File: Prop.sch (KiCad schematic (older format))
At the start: 12 parts

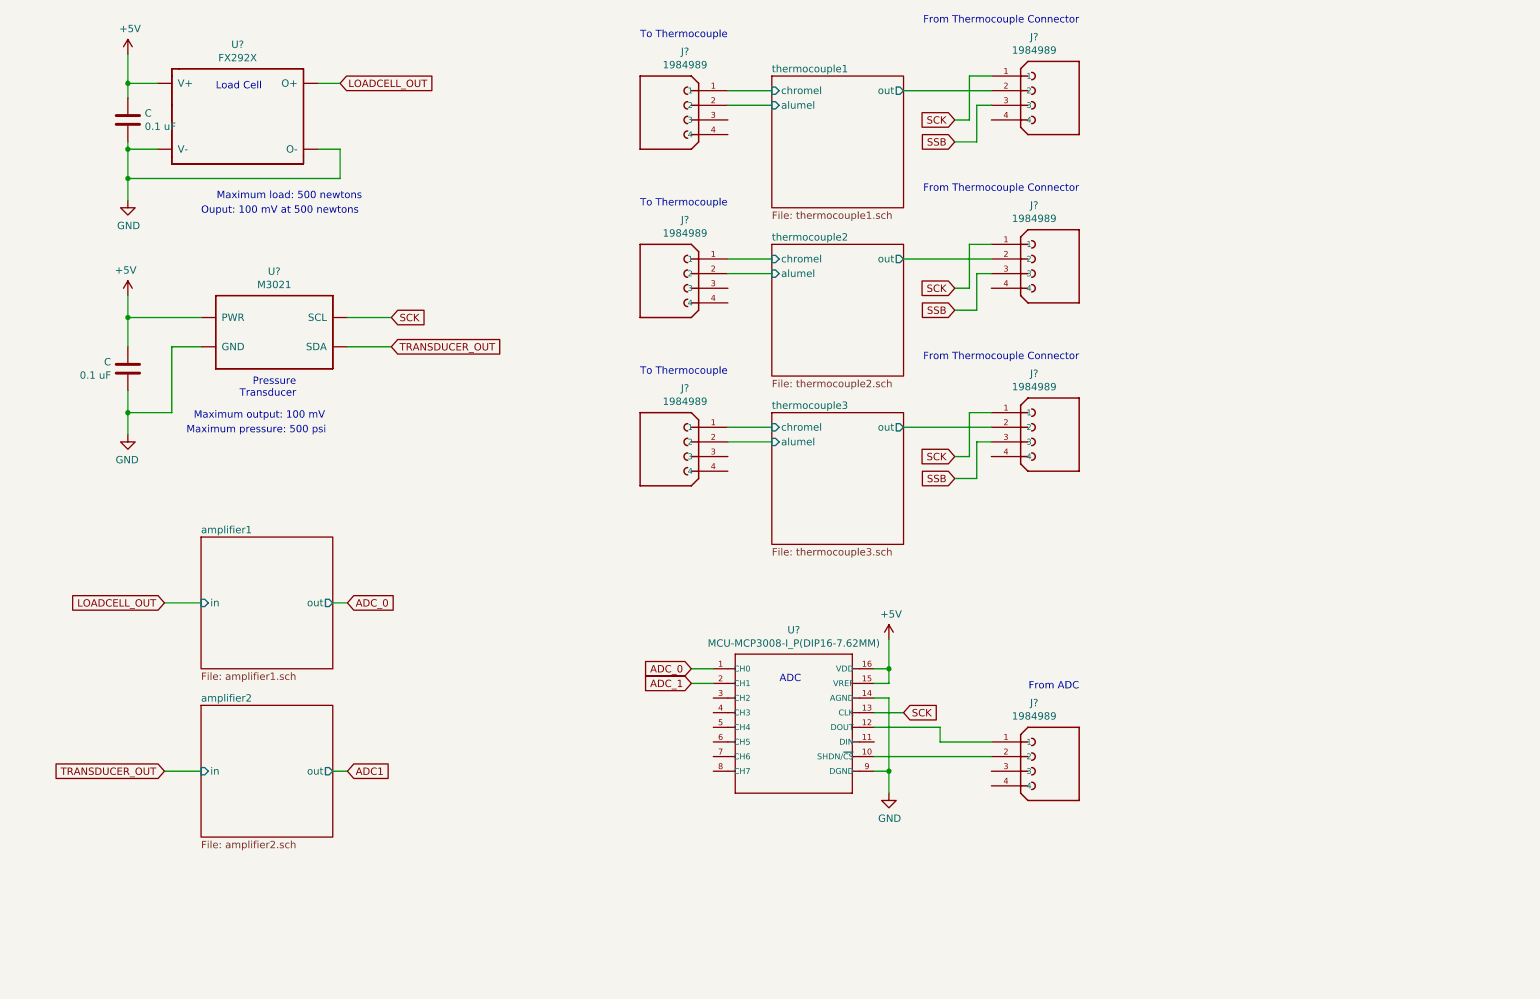
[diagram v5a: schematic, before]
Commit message: updated SCK
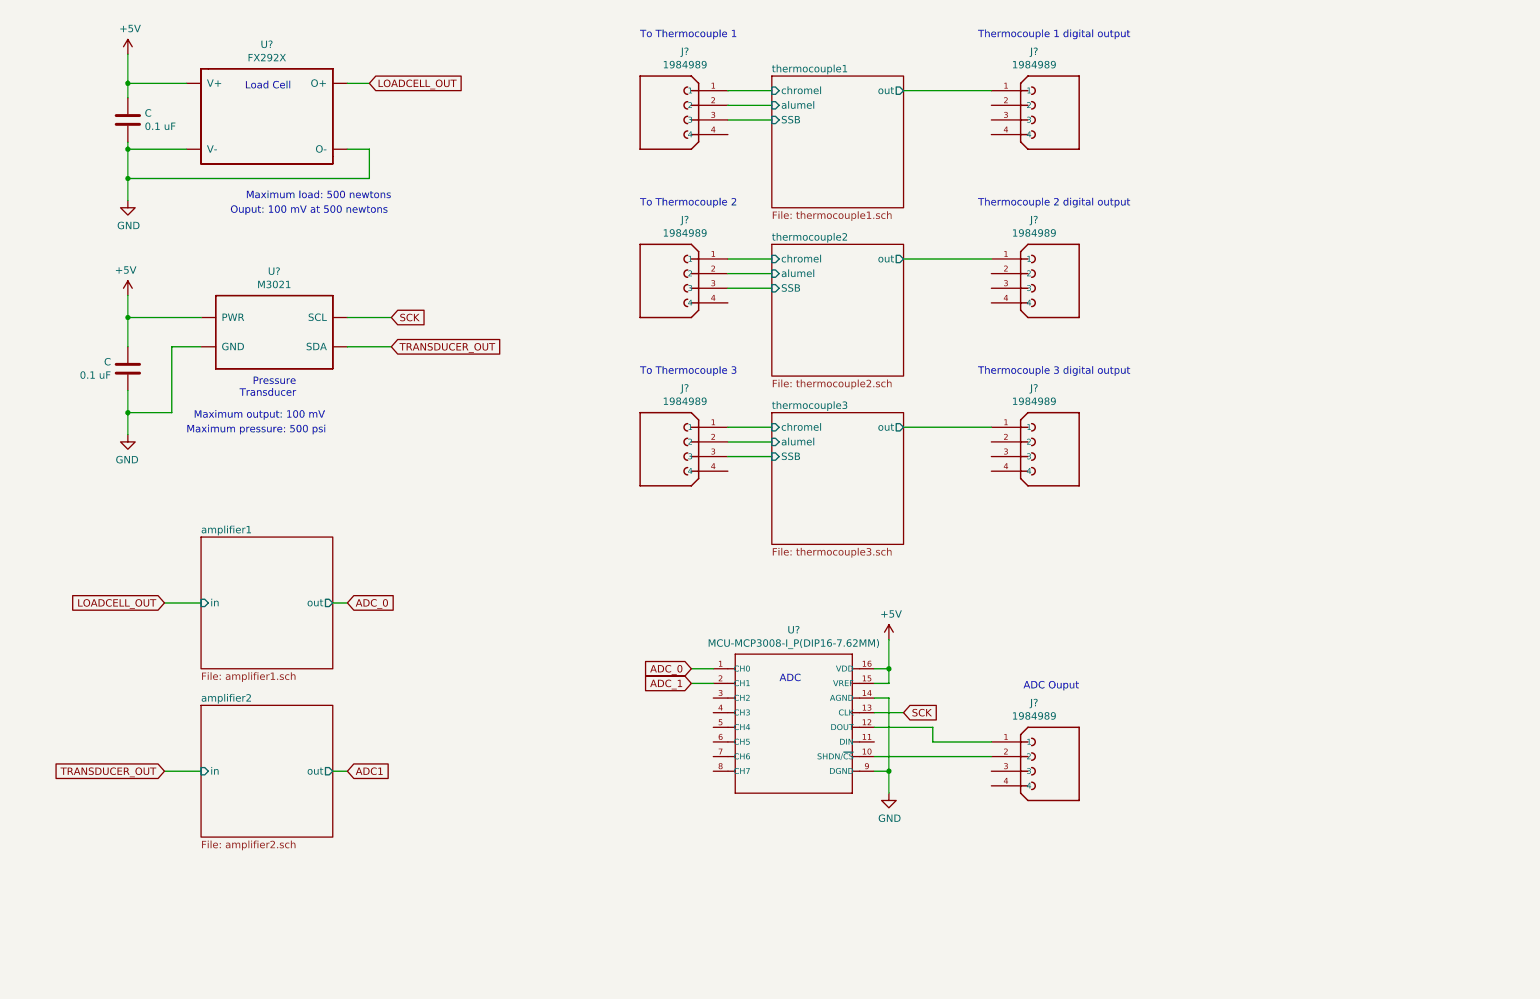
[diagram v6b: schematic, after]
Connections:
- net SCK: no longer J?.1, J?.1, J?.1
- net thermocouple1/out: now also J?.1; no longer J?.2
- net thermocouple2/out: now also J?.1; no longer J?.2
- net thermocouple3/out: now also J?.1; no longer J?.2
- net thermocouple1/SSB: now reaches J?.3
- net thermocouple2/SSB: now reaches J?.3
- net thermocouple3/SSB: now reaches J?.3
- removed net SSB: J?.3, J?.3, J?.3
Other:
- note added: "ADC Ouput"
- note added: "Thermocouple 1 digital output"
- note added: "Thermocouple 2 digital output"
- note added: "Thermocouple 3 digital output"
- note added: "To Thermocouple 1"
- note added: "To Thermocouple 2"
- note added: "To Thermocouple 3"
- note removed: "From ADC"
- note removed: "From Thermocouple Connector"
- note removed: "To Thermocouple"
- moved on the sheet: J?, U?
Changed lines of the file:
@@
 Connection ~ 1500 3400
 Wire Wire Line
-	2800 1150 2950 1150
+	3000 1150 3150 1150
 $Comp
 L power:+5V #PWR?
@@
 	1    0    0    -1
 $EndComp
-Text Notes 2100 1200 0    50   ~ 0
+Text Notes 2300 1200 0    50   ~ 0
 Load Cell
-Text GLabel 2950 1150 2    50   Input ~ 0
+Text GLabel 3150 1150 2    50   Input ~ 0
 LOADCELL_OUT
 $Comp
 L FX292X_Lib:FX292X U?
 U 1 1 603BDAFB
-P 2250 1250
-F 0 "U?" H 2250 1615 50  0000 C CNN
-F 1 "FX292X" H 2250 1524 50  0000 C CNN
-F 2 "" H 2250 1250 50  0001 C CNN
-F 3 "" H 2250 1250 50  0001 C CNN
-	1    2250 1250
+P 2450 1250
+F 0 "U?" H 2450 1615 50  0000 C CNN
+F 1 "FX292X" H 2450 1524 50  0000 C CNN
+F 2 "" H 2450 1250 50  0001 C CNN
+F 3 "" H 2450 1250 50  0001 C CNN
+	1    2450 1250
 	1    0    0    -1
 $EndComp
@@
 L 1984989:1984989 J?
 U 1 1 6041FC25
-P 7800 1200
-F 0 "J?" H 7907 1567 50  0000 C CNN
-F 1 "1984989" H 7907 1476 50  0000 C CNN
-F 2 "PHOENIX_1984989" H 7800 1200 50  0001 L BNN
-F 3 "" H 7800 1200 50  0001 L BNN
-F 4 "Phoenix Contact" H 7800 1200 50  0001 L BNN "MANUFACTURER"
-F 5 "2018-11-03" H 7800 1200 50  0001 L BNN "PARTREV"
-F 6 "13.1mm" H 7800 1200 50  0001 L BNN "MAXIMUM_PACKAGE_HEIGHT"
-F 7 "Manufacturer recommendations" H 7800 1200 50  0001 L BNN "STANDARD"
-	1    7800 1200
-	-1   0    0    -1
-$EndComp
-Text GLabel 7150 1400 0    50   Input ~ 0
-SCK
-Text GLabel 7150 1550 0    50   Input ~ 0
-SSB
+P 7800 1300
+F 0 "J?" H 7907 1667 50  0000 C CNN
+F 1 "1984989" H 7907 1576 50  0000 C CNN
+F 2 "PHOENIX_1984989" H 7800 1300 50  0001 L BNN
+F 3 "" H 7800 1300 50  0001 L BNN
+F 4 "Phoenix Contact" H 7800 1300 50  0001 L BNN "MANUFACTURER"
+F 5 "2018-11-03" H 7800 1300 50  0001 L BNN "PARTREV"
+F 6 "13.1mm" H 7800 1300 50  0001 L BNN "MAXIMUM_PACKAGE_HEIGHT"
+F 7 "Manufacturer recommendations" H 7800 1300 50  0001 L BNN "STANDARD"
+	1    7800 1300
+	-1   0    0    -1
+$EndComp
 $Comp
 L 1984989:1984989 J?
@@
 $EndComp
 Text Notes 5000 850  0    50   ~ 0
-To Thermocouple
-Text Notes 8000 750  2    50   ~ 0
-From Thermocouple Connector
+To Thermocouple 1
+Text Notes 8350 850  2    50   ~ 0
+Thermocouple 1 digital output
 Text Notes 8000 5300 2    50   ~ 0
-From ADC
+ADC Ouput
 $Comp
 L Device:C C
@@
 $EndComp
 Wire Wire Line
-	1500 950  1500 1150
-Wire Wire Line
-	1700 1150 1500 1150
-Wire Wire Line
-	1500 1600 1700 1600
-Wire Wire Line
-	1500 1600 1500 1550
-Wire Wire Line
-	1500 1250 1500 1150
-Connection ~ 1500 1150
-Wire Wire Line
-	1500 1600 1500 1800
-Connection ~ 1500 1600
-Wire Wire Line
-	2800 1600 2950 1600
-Wire Wire Line
-	2950 1600 2950 1800
-Wire Wire Line
-	2950 1800 1500 1800
-Connection ~ 1500 1800
-Wire Wire Line
-	1500 1800 1500 1950
+	3000 1600 3150 1600
+Wire Wire Line
+	3150 1600 3150 1800
 $Comp
 L MCU-MCP3008-I_P_DIP16-7.62MM_:MCU-MCP3008-I_P(DIP16-7.62MM) U?
@@
 Text Notes 6100 5250 2    50   ~ 0
 ADC
-Text Notes 3100 1950 2    50   ~ 0
+Text Notes 3300 1950 2    50   ~ 0
 Maximum load: 500 newtons
-Text Notes 2000 2050 0    50   ~ 0
+Text Notes 2200 2050 0    50   ~ 0
 Ouput: 100 mV at 500 newtons
 Text GLabel 5350 5150 0    50   Input ~ 0
@@
 F3 "chromel" I L 5900 1200 50
 F4 "out" O R 6800 1200 50
+F5 "SSB" I L 5900 1400 50
 $EndSheet
 $Sheet
@@
 F3 "alumel" I L 5900 2450 50
 F4 "out" O R 6800 2350 50
+F5 "SSB" I L 5900 2550 50
 $EndSheet
 $Sheet
@@
 F3 "alumel" I L 5900 3600 50
 F4 "out" O R 6800 3500 50
+F5 "SSB" I L 5900 3700 50
 $EndSheet
 $Comp
@@
 	5900 2450 5600 2450
 Text Notes 5000 2000 0    50   ~ 0
-To Thermocouple
+To Thermocouple 2
 $Comp
 L 1984989:1984989 J?
@@
 	5900 3600 5600 3600
 Text Notes 5000 3150 0    50   ~ 0
-To Thermocouple
-Wire Wire Line
-	7150 1400 7250 1400
-Wire Wire Line
-	7250 1400 7250 1100
-Wire Wire Line
-	7250 1100 7400 1100
-Wire Wire Line
-	7400 1300 7300 1300
-Wire Wire Line
-	7300 1300 7300 1550
-Wire Wire Line
-	7300 1550 7150 1550
-Wire Wire Line
-	7400 1200 6800 1200
+To Thermocouple 3
 $Comp
 L 1984989:1984989 J?
 U 1 1 6054FBA1
-P 7800 2350
-F 0 "J?" H 7907 2717 50  0000 C CNN
-F 1 "1984989" H 7907 2626 50  0000 C CNN
-F 2 "PHOENIX_1984989" H 7800 2350 50  0001 L BNN
-F 3 "" H 7800 2350 50  0001 L BNN
-F 4 "Phoenix Contact" H 7800 2350 50  0001 L BNN "MANUFACTURER"
-F 5 "2018-11-03" H 7800 2350 50  0001 L BNN "PARTREV"
-F 6 "13.1mm" H 7800 2350 50  0001 L BNN "MAXIMUM_PACKAGE_HEIGHT"
-F 7 "Manufacturer recommendations" H 7800 2350 50  0001 L BNN "STANDARD"
-	1    7800 2350
-	-1   0    0    -1
-$EndComp
-Text GLabel 7150 2550 0    50   Input ~ 0
-SCK
-Text GLabel 7150 2700 0    50   Input ~ 0
-SSB
-Text Notes 8000 1900 2    50   ~ 0
-From Thermocouple Connector
-Wire Wire Line
-	7150 2550 7250 2550
-Wire Wire Line
-	7250 2550 7250 2250
-Wire Wire Line
-	7250 2250 7400 2250
-Wire Wire Line
-	7400 2450 7300 2450
-Wire Wire Line
-	7300 2450 7300 2700
-Wire Wire Line
-	7300 2700 7150 2700
+P 7800 2450
+F 0 "J?" H 7907 2817 50  0000 C CNN
+F 1 "1984989" H 7907 2726 50  0000 C CNN
+F 2 "PHOENIX_1984989" H 7800 2450 50  0001 L BNN
+F 3 "" H 7800 2450 50  0001 L BNN
+F 4 "Phoenix Contact" H 7800 2450 50  0001 L BNN "MANUFACTURER"
+F 5 "2018-11-03" H 7800 2450 50  0001 L BNN "PARTREV"
+F 6 "13.1mm" H 7800 2450 50  0001 L BNN "MAXIMUM_PACKAGE_HEIGHT"
+F 7 "Manufacturer recommendations" H 7800 2450 50  0001 L BNN "STANDARD"
+	1    7800 2450
+	-1   0    0    -1
+$EndComp
+Text Notes 8350 2000 2    50   ~ 0
+Thermocouple 2 digital output
+$Comp
+L 1984989:1984989 J?
+U 1 1 605526CF
+P 7800 3600
+F 0 "J?" H 7907 3967 50  0000 C CNN
+F 1 "1984989" H 7907 3876 50  0000 C CNN
+F 2 "PHOENIX_1984989" H 7800 3600 50  0001 L BNN
+F 3 "" H 7800 3600 50  0001 L BNN
+F 4 "Phoenix Contact" H 7800 3600 50  0001 L BNN "MANUFACTURER"
+F 5 "2018-11-03" H 7800 3600 50  0001 L BNN "PARTREV"
+F 6 "13.1mm" H 7800 3600 50  0001 L BNN "MAXIMUM_PACKAGE_HEIGHT"
+F 7 "Manufacturer recommendations" H 7800 3600 50  0001 L BNN "STANDARD"
+	1    7800 3600
+	-1   0    0    -1
+$EndComp
+Text Notes 8350 3150 2    50   ~ 0
+Thermocouple 3 digital output
+Wire Wire Line
+	6600 5750 7400 5750
+Wire Wire Line
+	1500 950  1500 1150
+Wire Wire Line
+	1500 1550 1500 1600
+Wire Wire Line
+	1500 1150 1900 1150
+Connection ~ 1500 1150
+Wire Wire Line
+	1500 1150 1500 1250
+Wire Wire Line
+	1500 1600 1900 1600
+Connection ~ 1500 1600
+Wire Wire Line
+	1500 1600 1500 1800
+Wire Wire Line
+	1500 1800 3150 1800
+Connection ~ 1500 1800
+Wire Wire Line
+	1500 1800 1500 1950
+Wire Wire Line
+	5600 3700 5900 3700
+Wire Wire Line
+	6800 3500 7400 3500
 Wire Wire Line
 	7400 2350 6800 2350
-$Comp
-L 1984989:1984989 J?
-U 1 1 605526CF
-P 7800 3500
-F 0 "J?" H 7907 3867 50  0000 C CNN
-F 1 "1984989" H 7907 3776 50  0000 C CNN
-F 2 "PHOENIX_1984989" H 7800 3500 50  0001 L BNN
-F 3 "" H 7800 3500 50  0001 L BNN
-F 4 "Phoenix Contact" H 7800 3500 50  0001 L BNN "MANUFACTURER"
-F 5 "2018-11-03" H 7800 3500 50  0001 L BNN "PARTREV"
-F 6 "13.1mm" H 7800 3500 50  0001 L BNN "MAXIMUM_PACKAGE_HEIGHT"
-F 7 "Manufacturer recommendations" H 7800 3500 50  0001 L BNN "STANDARD"
-	1    7800 3500
-	-1   0    0    -1
-$EndComp
-Text GLabel 7150 3700 0    50   Input ~ 0
-SCK
-Text GLabel 7150 3850 0    50   Input ~ 0
-SSB
-Text Notes 8000 3050 2    50   ~ 0
-From Thermocouple Connector
-Wire Wire Line
-	7150 3700 7250 3700
-Wire Wire Line
-	7250 3700 7250 3400
-Wire Wire Line
-	7250 3400 7400 3400
-Wire Wire Line
-	7400 3600 7300 3600
-Wire Wire Line
-	7300 3600 7300 3850
-Wire Wire Line
-	7300 3850 7150 3850
-Wire Wire Line
-	7400 3500 6800 3500
-Wire Wire Line
-	6600 5550 7050 5550
-Wire Wire Line
-	7050 5550 7050 5650
-Wire Wire Line
-	6600 5750 7400 5750
-Wire Wire Line
-	7050 5650 7400 5650
+Wire Wire Line
+	5600 2550 5900 2550
+Wire Wire Line
+	6800 1200 7400 1200
+Wire Wire Line
+	5600 1400 5900 1400
+Wire Wire Line
+	6600 5550 7000 5550
+Wire Wire Line
+	7000 5550 7000 5650
+Wire Wire Line
+	7000 5650 7400 5650
 $EndSCHEMATC
